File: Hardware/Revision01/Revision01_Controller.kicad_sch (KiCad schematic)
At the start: 4 parts, among them U1 NUCLEO-L476RG, U10 NCP1117LPST50T3G

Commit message: todays review session
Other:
- removed sheet NUCLEO-L476RG_Top
- note added: "THIS DOES NOT BELONG IN CONTROLLER"
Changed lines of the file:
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@@
 		)
 	)
+	(text "THIS DOES NOT BELONG IN CONTROLLER"
+		(exclude_from_sim no)
+		(at 253.238 23.876 0)
+		(effects
+			(font
+				(size 0.635 0.635)
+				(color 255 0 0 1)
+			)
+		)
+	)
 	(text "+3.3V <JP6> VDD"
 		(exclude_from_sim no)
@@
 	)
 	(hierarchical_label "+V_BATT"
-		(shape output)
+		(shape input)
 		(at 198.12 30.48 180)
 		(effects
@@
 				)
 			)
-		)
-	)
-	(sheet
-		(at 139.065 35.56)
-		(size 36.83 7.62)
-		(exclude_from_sim yes)
-		(in_bom no)
-		(on_board no)
-		(dnp yes)
-		(fields_autoplaced yes)
-		(stroke
-			(width 0.1524)
-			(type solid)
-		)
-		(fill
-			(color 0 0 0 0.0000)
-		)
-		(property "Sheetname" "NUCLEO-L476RG_Top"
-			(at 139.065 34.8484 0)
-			(effects
-				(font
-					(size 1.27 1.27)
-				)
-				(justify left bottom)
-			)
-		)
-		(property "Sheetfile" "NUCLEO-L476RG_Top.kicad_sch"
-			(at 139.065 43.7646 0)
-			(effects
-				(font
-					(size 1.27 1.27)
-				)
-				(justify left top)
-			)
-		)
-		(instances
-			(project "Revision01"
-				(path "/955cc99e-a129-42cf-abc7-aa99813fdb5f/00000000-0000-0000-0000-00005ea70ac3"
-					(page "4")
-				)
-			)

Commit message: implemented feedback
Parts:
- removed C46, C47: 10uF, Capacitor_SMD:C_1206_3216Metric, symbol Device:C
- removed U10: NCP1117LPST50T3G, NCP1117LPST50T3G:SOT230P700X180-4N, symbol NCP1117LPST50T3G:NCP1117LPST50T3G
- added TP38, TP54, TP55, TP56, TP57, TP58, TP59: TestPoint, symbol Connector:TestPoint
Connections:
- net +3V3_NUCLEO: now also TP38.1
- net BOOT0: now also TP54.1
- net PA15/JTDI/TIM2_CH1_ETR/SPI1_NSS renamed PA15/TIM2_CH1_ETR/SPI1_NSS
- net PA5/SPI1_SCK/ADC12_IN5 renamed PA5_LED2/SPI1_SCK/ADC12_IN5
- net PB1 renamed PB1/ADC12_IN9/TIM3_CH4/TIM1_CH3N
- net PB4/JNTRST/TIM3_CH1/PB4/SPI1_MISO renamed PB4/TIM3_CH1/PB4/SPI1_MISO
- net PC2 renamed PC2/ADC12_IN12
- net PC3 renamed PC3/ADC12_IN13
- net STLK_RX_USART2 renamed PA3/USART2_RX/ADC12_IN3/TIM2_CH4
- net PA3/USART2_RX/ADC12_IN3/TIM2_CH4: now also TP59.1
- net STLK_TX_USART2 renamed PA2/USART2_TX/ADC12_IN2/TIM2_CH3
- net PA2/USART2_TX/ADC12_IN2/TIM2_CH3: now also TP58.1
- net SWCLK renamed PA14/JTCK/SWCLK
- net PA14/JTCK/SWCLK: now also TP56.1
- net SWDIO renamed PA13/JTMS/SWDIO
- net PA13/JTMS/SWDIO: now also TP55.1
- net TRACESWO renamed PB3/JTDO/TIM2_CH2/PB3/TRACESWO/SPI1_SCK
- net PB3/JTDO/TIM2_CH2/PB3/TRACESWO/SPI1_SCK: now also TP57.1
- no-connect marks 42 -> 17
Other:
- note added: "(NC)"
- note added: "10K PullDown"
- note added: "OSC32_IN"
- note added: "OSC32_OUT"
- note added: "STLK_RX = USART2_RX"
- note added: "STLK_TX = USART2_TX"
- note added: "SWCLK"
- note added: "SWDIO"
- note added: "TRACESWO"
- note added: "VDD"
- note removed: "Remove the power jumper on nucleo board before using this daughterboard"
- note removed: "THIS DOES NOT BELONG IN CONTROLLER"

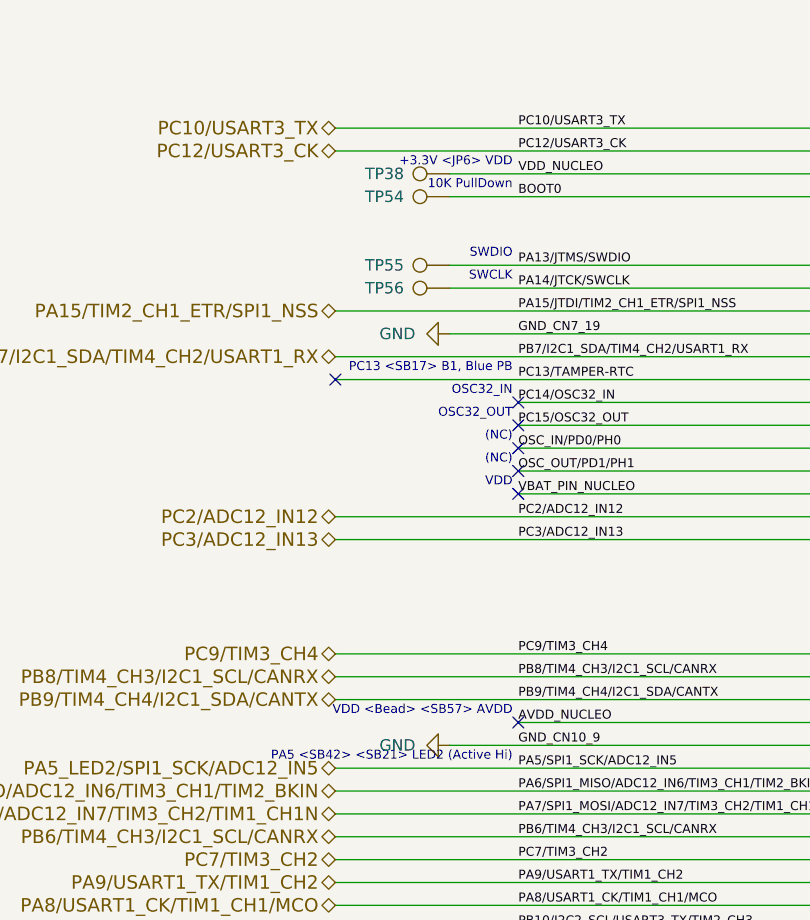
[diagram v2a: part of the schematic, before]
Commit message: some additional footprints assigned,
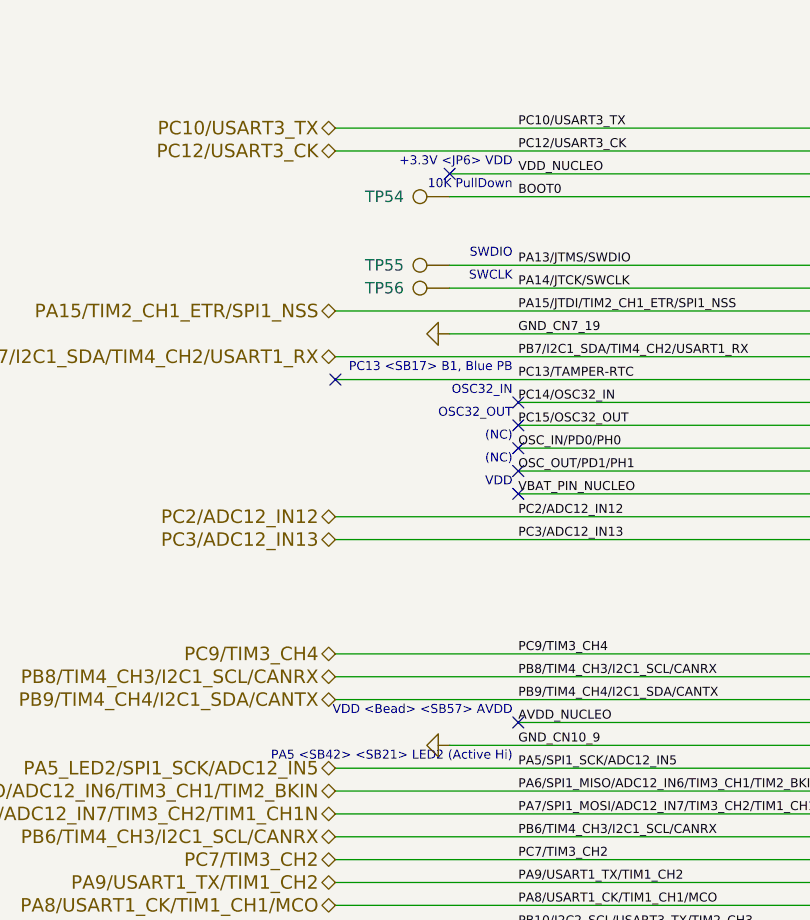
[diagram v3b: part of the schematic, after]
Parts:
- removed TP38: TestPoint, symbol Connector:TestPoint
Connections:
- no-connect marks 17 -> 18

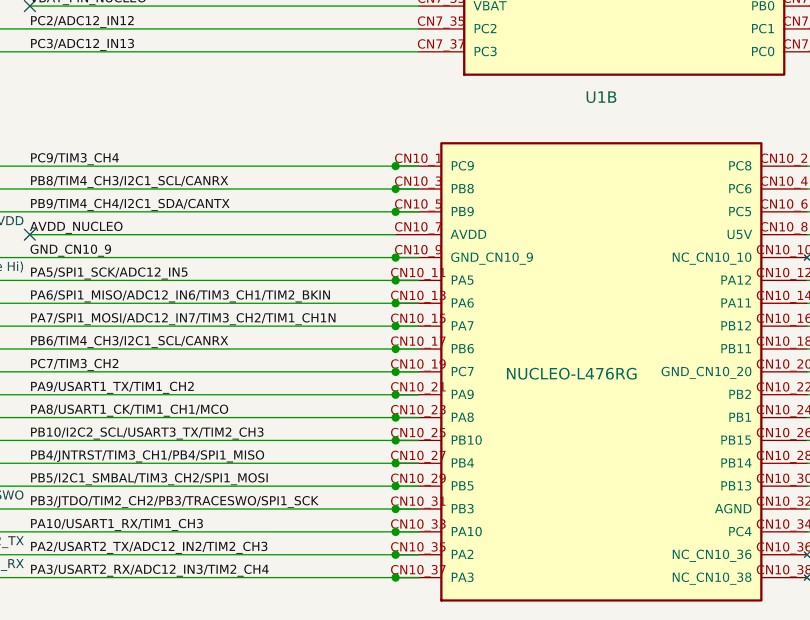
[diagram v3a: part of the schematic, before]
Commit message: added netclasses again changed power to be globally used strain gauges symbol created and added to schematic
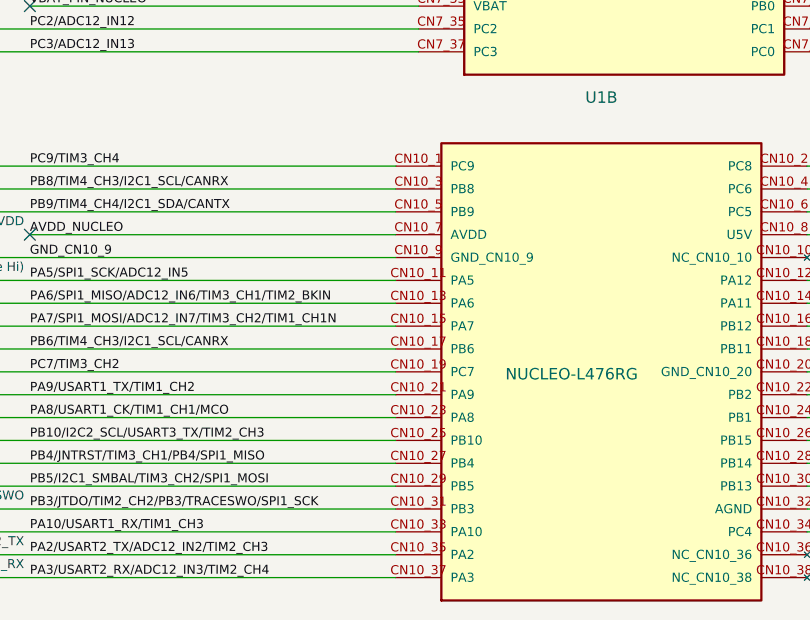
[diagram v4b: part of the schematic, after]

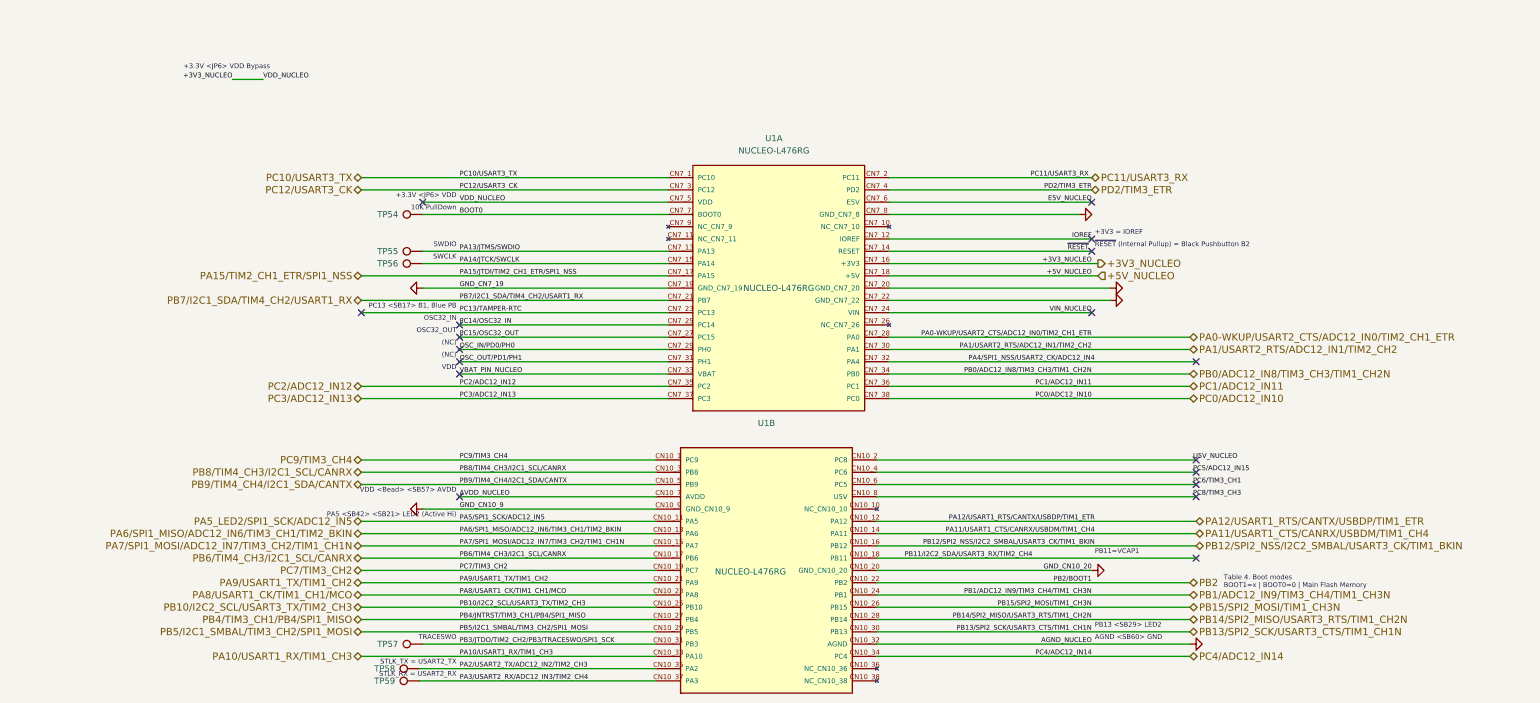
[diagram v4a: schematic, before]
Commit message: Reworked Controller sheet to nucleo L476RG
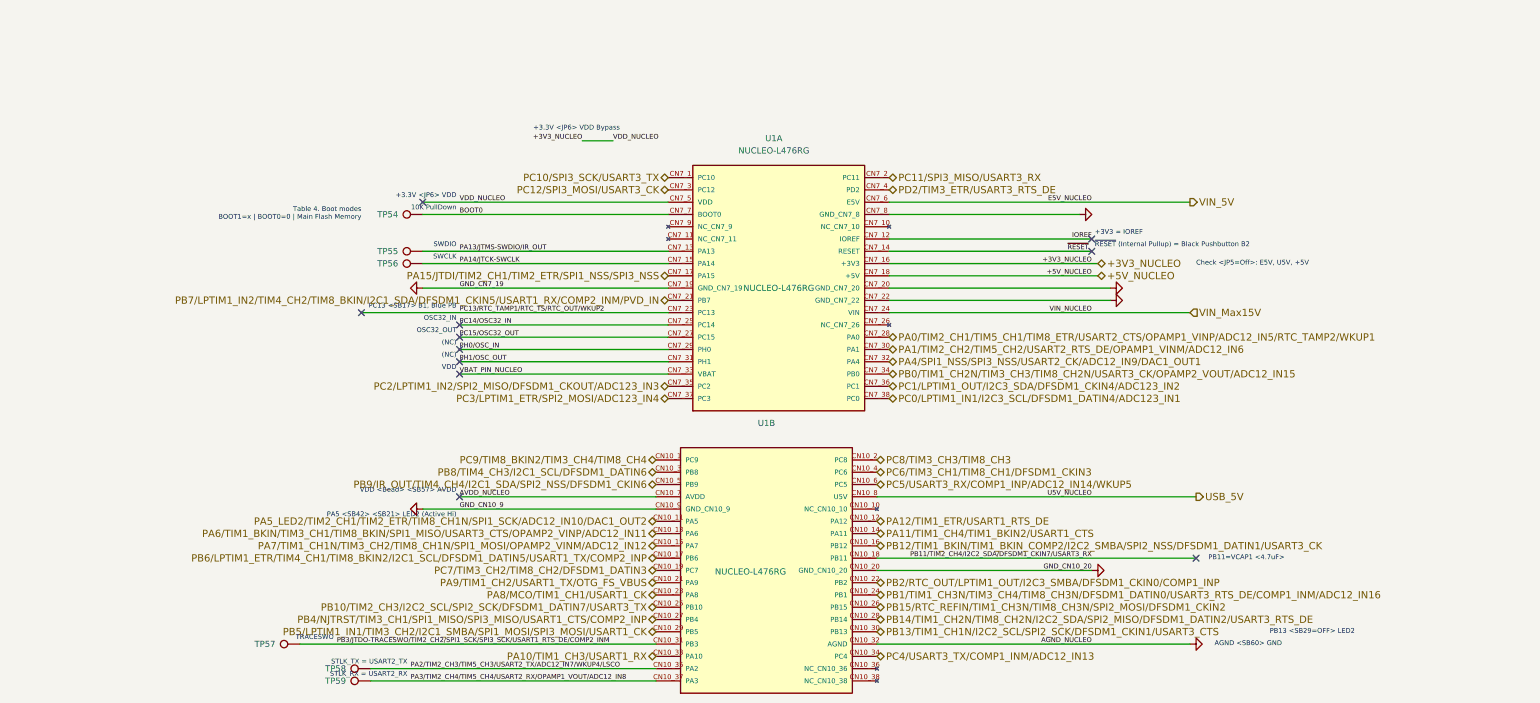
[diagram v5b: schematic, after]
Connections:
- net E5V_NUCLEO renamed VIN_5V
- net OSC_IN/PD0/PH0 renamed PH0/OSC_IN
- net OSC_OUT/PD1/PH1 renamed PH1/OSC_OUT
- net PA0-WKUP/USART2_CTS/ADC12_IN0/TIM2_CH1_ETR renamed PA0/TIM2_CH1/TIM5_CH1/TIM8_ETR/USART2_CTS/OPAMP1_VINP/ADC12_IN5/RTC_TAMP2/WKUP1
- net PA10/USART1_RX/TIM1_CH3 renamed PA10/TIM1_CH3/USART1_RX
- net PA11/USART1_CTS/CANRX/USBDM/TIM1_CH4 renamed PA11/TIM1_CH4/TIM1_BKIN2/USART1_CTS
- net PA12/USART1_RTS/CANTX/USBDP/TIM1_ETR renamed PA12/TIM1_ETR/USART1_RTS_DE
- net PA13/JTMS/SWDIO renamed PA13/JTMS-SWDIO/IR_OUT
- net PA14/JTCK/SWCLK renamed PA14/JTCK-SWCLK
- net PA15/TIM2_CH1_ETR/SPI1_NSS renamed PA15/JTDI/TIM2_CH1/TIM2_ETR/SPI1_NSS/SPI3_NSS
- net PA1/USART2_RTS/ADC12_IN1/TIM2_CH2 renamed PA1/TIM2_CH2/TIM5_CH2/USART2_RTS_DE/OPAMP1_VINM/ADC12_IN6
- net PA2/USART2_TX/ADC12_IN2/TIM2_CH3 renamed PA2/TIM2_CH3/TIM5_CH3/USART2_TX/ADC12_IN7/WKUP4/LSCO
- net PA3/USART2_RX/ADC12_IN3/TIM2_CH4 renamed PA3/TIM2_CH4/TIM5_CH4/USART2_RX/OPAMP1_VOUT/ADC12_IN8
- net PA4/SPI1_NSS/USART2_CK/ADC12_IN4 renamed PA4/SPI1_NSS/SPI3_NSS/USART2_CK/ADC12_IN9/DAC1_OUT1
- net PA5_LED2/SPI1_SCK/ADC12_IN5 renamed PA5_LED2/TIM2_CH1/TIM2_ETR/TIM8_CH1N/SPI1_SCK/ADC12_IN10/DAC1_OUT2
- net PA6/SPI1_MISO/ADC12_IN6/TIM3_CH1/TIM2_BKIN renamed PA6/TIM1_BKIN/TIM3_CH1/TIM8_BKIN/SPI1_MISO/USART3_CTS/OPAMP2_VINP/ADC12_IN11
- net PA7/SPI1_MOSI/ADC12_IN7/TIM3_CH2/TIM1_CH1N renamed PA7/TIM1_CH1N/TIM3_CH2/TIM8_CH1N/SPI1_MOSI/OPAMP2_VINM/ADC12_IN12
- net PA8/USART1_CK/TIM1_CH1/MCO renamed PA8/MCO/TIM1_CH1/USART1_CK
- net PA9/USART1_TX/TIM1_CH2 renamed PA9/TIM1_CH2/USART1_TX/OTG_FS_VBUS
- net PB0/ADC12_IN8/TIM3_CH3/TIM1_CH2N renamed PB0/TIM1_CH2N/TIM3_CH3/TIM8_CH2N/USART3_CK/OPAMP2_VOUT/ADC12_IN15
- net PB10/I2C2_SCL/USART3_TX/TIM2_CH3 renamed PB10/TIM2_CH3/I2C2_SCL/SPI2_SCK/DFSDM1_DATIN7/USART3_TX
- net PB11/I2C2_SDA/USART3_RX/TIM2_CH4 renamed PB11/TIM2_CH4/I2C2_SDA/DFSDM1_CKIN7/USART3_RX
- net PB12/SPI2_NSS/I2C2_SMBAL/USART3_CK/TIM1_BKIN renamed PB12/TIM1_BKIN/TIM1_BKIN_COMP2/I2C2_SMBA/SPI2_NSS/DFSDM1_DATIN1/USART3_CK
- net PB13/SPI2_SCK/USART3_CTS/TIM1_CH1N renamed PB13/TIM1_CH1N/I2C2_SCL/SPI2_SCK/DFSDM1_CKIN1/USART3_CTS
- net PB14/SPI2_MISO/USART3_RTS/TIM1_CH2N renamed PB14/TIM1_CH2N/TIM8_CH2N/I2C2_SDA/SPI2_MISO/DFSDM1_DATIN2/USART3_RTS_DE
- net PB15/SPI2_MOSI/TIM1_CH3N renamed PB15/RTC_REFIN/TIM1_CH3N/TIM8_CH3N/SPI2_MOSI/DFSDM1_CKIN2
- net PB1/ADC12_IN9/TIM3_CH4/TIM1_CH3N renamed PB1/TIM1_CH3N/TIM3_CH4/TIM8_CH3N/DFSDM1_DATIN0/USART3_RTS_DE/COMP1_INM/ADC12_IN16
- net PB2 renamed PB2/RTC_OUT/LPTIM1_OUT/I2C3_SMBA/DFSDM1_CKIN0/COMP1_INP
- net PB3/JTDO/TIM2_CH2/PB3/TRACESWO/SPI1_SCK renamed PB3/JTDO-TRACESWO/TIM2_CH2/SPI1_SCK/SPI3_SCK/USART1_RTS_DE/COMP2_INM
- net PB4/TIM3_CH1/PB4/SPI1_MISO renamed PB4/NJTRST/TIM3_CH1/SPI1_MISO/SPI3_MISO/USART1_CTS/COMP2_INP
- net PB5/I2C1_SMBAL/TIM3_CH2/SPI1_MOSI renamed PB5/LPTIM1_IN1/TIM3_CH2/I2C1_SMBA/SPI1_MOSI/SPI3_MOSI/USART1_CK
- net PB6/TIM4_CH3/I2C1_SCL/CANRX renamed PB6/LPTIM1_ETR/TIM4_CH1/TIM8_BKIN2/I2C1_SCL/DFSDM1_DATIN5/USART1_TX/COMP2_INP
- net PB7/I2C1_SDA/TIM4_CH2/USART1_RX renamed PB7/LPTIM1_IN2/TIM4_CH2/TIM8_BKIN/I2C1_SDA/DFSDM1_CKIN5/USART1_RX/COMP2_INM/PVD_IN
- net PB8/TIM4_CH3/I2C1_SCL/CANRX renamed PB8/TIM4_CH3/I2C1_SCL/DFSDM1_DATIN6
- net PB9/TIM4_CH4/I2C1_SDA/CANTX renamed PB9/IR_OUT/TIM4_CH4/I2C1_SDA/SPI2_NSS/DFSDM1_CKIN6
- net PC0/ADC12_IN10 renamed PC0/LPTIM1_IN1/I2C3_SCL/DFSDM1_DATIN4/ADC123_IN1
- net PC10/USART3_TX renamed PC10/SPI3_SCK/USART3_TX
- net PC11/USART3_RX renamed PC11/SPI3_MISO/USART3_RX
- net PC12/USART3_CK renamed PC12/SPI3_MOSI/USART3_CK
- net PC13/TAMPER-RTC renamed PC13/RTC_TAMP1/RTC_TS/RTC_OUT/WKUP2
- net PC1/ADC12_IN11 renamed PC1/LPTIM1_OUT/I2C3_SDA/DFSDM1_CKIN4/ADC123_IN2
- net PC2/ADC12_IN12 renamed PC2/LPTIM1_IN2/SPI2_MISO/DFSDM1_CKOUT/ADC123_IN3
- net PC3/ADC12_IN13 renamed PC3/LPTIM1_ETR/SPI2_MOSI/ADC123_IN4
- net PC4/ADC12_IN14 renamed PC4/USART3_TX/COMP1_INM/ADC12_IN13
- net PC5/ADC12_IN15 renamed PC6/TIM3_CH1/TIM8_CH1/DFSDM1_CKIN3
- net PC6/TIM3_CH1 renamed PC5/USART3_RX/COMP1_INP/ADC12_IN14/WKUP5
- net PC7/TIM3_CH2 renamed PC7/TIM3_CH2/TIM8_CH2/DFSDM1_DATIN3
- net PC8/TIM3_CH3 renamed USB_5V
- net PC9/TIM3_CH4 renamed PC9/TIM8_BKIN2/TIM3_CH4/TIM8_CH4
- net PD2/TIM3_ETR renamed PD2/TIM3_ETR/USART3_RTS_DE
- net U5V_NUCLEO renamed PC8/TIM3_CH3/TIM8_CH3
- net VIN_NUCLEO renamed VIN_Max15V
- no-connect marks 18 -> 11
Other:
- note added: "Check <JP5=Off>: E5V, U5V, +5V"
- note added: "PB11=VCAP1 <4.7uF>"
- note added: "PB13 <SB29=OFF> LED2"
- note removed: "PB11=VCAP1"
- note removed: "PB13 <SB29> LED2"
- moved on the sheet: TP57, TP58, TP59
